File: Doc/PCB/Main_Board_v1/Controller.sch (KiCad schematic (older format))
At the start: 37 parts, among them J10 PTR1, J11 UART, J12 BUZZER, J7 Conn_01x02, J8 SP3, J9 SP2, Q2 IRLZ34N, Q3 IRLZ34N, U4 7805, U5 XPRESS-40, U6 LCD

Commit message: New Schemartics. Clean up monitor
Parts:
- removed C12: 4.7uF 50V, Capacitor_THT:C_Rect_L9.0mm_W3.3mm_P7.50mm_MKT, symbol Device:C
- removed C13: 100nF, Capacitor_THT:C_Rect_L9.0mm_W3.3mm_P7.50mm_MKT, symbol Device:C
- removed J7: Conn_01x02, Connector_PinHeader_2.54mm:PinHeader_1x02_P2.54mm_Horizontal, symbol Connector_Generic:Conn_01x02
- removed R14: 100, Resistor_THT:R_Axial_DIN0207_L6.3mm_D2.5mm_P10.16mm_Horizontal, symbol Device:R
- removed RV1: 5k, Resistor_THT:R_Axial_DIN0207_L6.3mm_D2.5mm_P10.16mm_Horizontal, symbol Device:R_POT
- removed U4: 7805, Package_TO_SOT_THT:TO-220-3_Vertical, symbol Power_Management:7805
- removed U5: XPRESS-40, symbol MCU_Microchip_PIC18:XPRESS-40
- removed U6: LCD, Connector_PinHeader_2.54mm:PinHeader_1x04_P2.54mm_Vertical, symbol LCD:LCD
- added C15: 4.7uF 50V, Capacitor_THT:CP_Radial_D5.0mm_P2.50mm, symbol Device:C
- added C16: 100nF, Capacitor_THT:C_Rect_L9.0mm_W3.3mm_P7.50mm_MKT, symbol Device:C
- added J12: I2C Interface LCD, Connector_PinHeader_2.54mm:PinHeader_1x04_P2.54mm_Vertical, symbol Connector:Conn_01x04_Male
- added J7: TE_3.5mm_Screwless_P2, Ventilator:PinHeader_1x02_Screwless_3.5mm, symbol Ventilator:TE_3.5mm_Screwless_P2
- added R15, R17: 470, Resistor_THT:R_Axial_DIN0207_L6.3mm_D2.5mm_P10.16mm_Horizontal, symbol Device:R
- added U4: LM7805_TO220, Package_TO_SOT_THT:TO-220-3_Vertical, symbol Regulator_Linear:LM7805_TO220
- added U5: XPRESS-40, Ventilator:EXPRESS-40_DIP_40, symbol Ventilator:XPRESS-40
- D2, D3: value 1N4001 -> 1N4007
- J10: footprint (none) -> Connector_PinHeader_2.54mm:PinHeader_1x03_P2.54mm_Vertical
- J11: footprint Connector_PinHeader_2.54mm:PinHeader_1x03_P2.54mm_Horizontal -> Connector_PinHeader_2.54mm:PinHeader_1x03_P2.54mm_Vertical
- J13: renamed from J12; value BUZZER -> BUZZER_C; footprint Connector_PinHeader_2.54mm:PinHeader_1x02_P2.54mm_Horizontal -> Connector_PinHeader_2.54mm:PinHeader_1x02_P2.54mm_Vertical
- J8, J9: footprint (none) -> Connector_PinHeader_2.54mm:PinHeader_1x02_P2.54mm_Vertical
- R13: renamed from R11; value R -> 50
- renumbered C15 to C17, C16 to C18, C17 to C19, R12 to R14, R13 to R16, R15 to R18, R16 to R19, R17 to R20, R18 to R21, R19 to R22, R20 to R23
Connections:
- net labels added: +12V_C, +5V_C, LCD_SCL, LCD_SDA
- net labels removed: +12V, +5V
- wire segments 176 -> 163
- no-connect marks 16 -> 19
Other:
- moved on the sheet: C19

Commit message: Update in the PCB design. New docs and images
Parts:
- removed J10: PTR1, Connector_PinHeader_2.54mm:PinHeader_1x03_P2.54mm_Vertical, symbol Connector:Conn_01x03_Male
- removed J8: SP3, Connector_PinHeader_2.54mm:PinHeader_1x02_P2.54mm_Vertical, symbol Connector:Screw_Terminal_01x02
- removed J9: SP2, Connector_PinHeader_2.54mm:PinHeader_1x02_P2.54mm_Vertical, symbol Connector:Screw_Terminal_01x02
- removed TP10: IP, Connector_PinHeader_2.54mm:PinHeader_1x02_P2.54mm_Vertical, symbol Connector:TestPoint_2Pole
- removed TP4: LED Breath, Connector_PinHeader_2.54mm:PinHeader_1x02_P2.54mm_Vertical, symbol Connector:TestPoint_2Pole
- removed TP5: Breath, Connector_PinHeader_2.54mm:PinHeader_1x02_P2.54mm_Vertical, symbol Connector:TestPoint_2Pole
- removed TP6: +, Connector_PinHeader_2.54mm:PinHeader_1x02_P2.54mm_Vertical, symbol Connector:TestPoint_2Pole
- removed TP7: -, Connector_PinHeader_2.54mm:PinHeader_1x02_P2.54mm_Vertical, symbol Connector:TestPoint_2Pole
- removed TP8: BPM, Connector_PinHeader_2.54mm:PinHeader_1x02_P2.54mm_Vertical, symbol Connector:TestPoint_2Pole
- removed TP9: EP, Connector_PinHeader_2.54mm:PinHeader_1x02_P2.54mm_Vertical, symbol Connector:TestPoint_2Pole
- added C22, C23, C24, C25, C26, C27: 1uF, Capacitor_THT:C_Rect_L7.0mm_W2.5mm_P5.00mm, symbol Device:C
- added C28, C29, C?: 100nF, Capacitor_THT:C_Rect_L9.0mm_W3.3mm_P7.50mm_MKT, symbol Device:C
- added J10: BPM, Ventilator:PushButton, symbol Ventilator:Button
- added J16: IP, Ventilator:PushButton, symbol Ventilator:Button
- added J17: -, Ventilator:PushButton, symbol Ventilator:Button
- added J18: BREATH, Ventilator:PushButton_LED, symbol Ventilator:Button_LED
- added J19: EP, Ventilator:PushButton, symbol Ventilator:Button
- added J20: +, Ventilator:PushButton, symbol Ventilator:Button
- added J8: SV2, Ventilator:PinHeader_1x02_Screwless_3.5mm, symbol Ventilator:TE_3.5mm_Screwless_P2
- added J9: SV3, Ventilator:PinHeader_1x02_Screwless_3.5mm, symbol Ventilator:TE_3.5mm_Screwless_P2
- added J?: VOL, Ventilator:PushButton, symbol Ventilator:Button
- added J?: VOL_MAX, Ventilator:PushButton, symbol Ventilator:Button
- added J?: VOL_MIN, Ventilator:PushButton, symbol Ventilator:Button
- added R26: 50, Resistor_THT:R_Axial_DIN0207_L6.3mm_D2.5mm_P10.16mm_Horizontal, symbol Device:R
- added R27, R28, R? (x3): 10k, Resistor_THT:R_Axial_DIN0207_L6.3mm_D2.5mm_P10.16mm_Horizontal, symbol Device:R
- added R29: 470, Resistor_THT:R_Axial_DIN0207_L6.3mm_D2.5mm_P10.16mm_Horizontal, symbol Device:R
- added S3, S4: MPXV5004DP, Ventilator:1351-01, symbol Ventilator:MPXV5004DP
- added TP5, TP6, TP7, TP8: TestPoint, Ventilator:LCD_DRILL, symbol Connector:TestPoint
- C17: value 1uF -> 100nF; footprint Capacitor_THT:C_Rect_L7.0mm_W2.5mm_P5.00mm -> Capacitor_THT:C_Rect_L9.0mm_W3.3mm_P7.50mm_MKT
- R13: value 50 -> 470
- R14: value R -> 50
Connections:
- net labels added: PR2, PR3, SV2, SV3
- wire segments 163 -> 248
- no-connect marks 19 -> 14
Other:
- moved on the sheet: J13, R16

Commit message: First placement of board
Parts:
- added J24: Conn_01x08, Connector_PinHeader_2.54mm:PinHeader_1x08_P2.54mm_Horizontal, symbol Connector_Generic:Conn_01x08
- added R36: 10k, Resistor_THT:R_Axial_DIN0207_L6.3mm_D2.5mm_P10.16mm_Horizontal, symbol Device:R
- C14, C16, C17, C19, C28, C29: value 100nF -> 100nF - 100V; footprint Capacitor_THT:C_Rect_L9.0mm_W3.3mm_P7.50mm_MKT -> Capacitor_THT:C_Rect_L7.2mm_W2.5mm_P5.00mm_FKS2_FKP2_MKS2_MKP2
- C15: footprint Capacitor_THT:CP_Radial_D5.0mm_P2.50mm -> Capacitor_THT:CP_Radial_D5.0mm_P2.00mm
- C18, C22, C23, C24, C25, C26, C27: footprint Capacitor_THT:C_Rect_L7.0mm_W2.5mm_P5.00mm -> Capacitor_THT:C_Rect_L13.0mm_W4.0mm_P10.00mm_FKS3_FKP3_MKS4
- C30: renamed from C?; value 100nF -> 100nF - 100V; footprint Capacitor_THT:C_Rect_L9.0mm_W3.3mm_P7.50mm_MKT -> Capacitor_THT:C_Rect_L7.2mm_W2.5mm_P5.00mm_FKS2_FKP2_MKS2_MKP2
- J12: value I2C Interface LCD -> I2C Interface LCD_C; footprint Connector_PinHeader_2.54mm:PinHeader_1x04_P2.54mm_Vertical -> Ventilator:PH_4_pol
- gave numbers to parts that had none: 6
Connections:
- net +5V_C: now also J24.2 (Pin_2), R36.1
- net GND: now also J24.3 (Pin_3)
- net nMCLR_C: now reaches U5.1 (RE3)
- net nMCLR_C: now also J24.1 (Pin_1), R36.2
- net ICSPCLK_C: now reaches U5.39 (TGCLK)
- net ICSPCLK_C: now also J24.5 (Pin_5)
- net ICSPDAT_C: now reaches U5.40 (TGDAT)
- net ICSPDAT_C: now also J24.4 (Pin_4)
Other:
- moved on the sheet: C29, J12, R15, R17

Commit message: Update in PCB: Schematic and Layout
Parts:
- added TP10, TP11, TP12, TP13: TestPoint, Ventilator:LCD_DRILL, symbol Connector:TestPoint
- Q2, Q3: value IRLZ34N -> STP24NF10
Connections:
- net GND: now also TP10.1, TP11.1, TP12.1, TP13.1
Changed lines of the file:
@@
 AR Path="/5E9339D0/5EC06140" Ref="Q2"  Part="1"
 F 0 "Q2" H 2954 5096 50  0000 L CNN
-F 1 "IRLZ34N" H 2954 5005 50  0000 L CNN
+F 1 "STP24NF10 " H 2954 5005 50  0000 L CNN
 F 2 "Package_TO_SOT_THT:TO-220-3_Vertical" H 3000 4975 50  0001 L CIN
-F 3 "http://www.infineon.com/dgdl/irlz34npbf.pdf?fileId=5546d462533600a40153567206892720" H 2750 5050 50  0001 L CNN
+F 3 "https://es.rs-online.com/web/p/mosfet/6875377/" H 2750 5050 50  0001 L CNN
 	1    2750 5050
 	-1   0    0    -1
@@
 F 1 "SV2" V 1974 4267 50  0000 C CNN
 F 2 "Ventilator:PinHeader_1x02_Screwless_3.5mm" H 1650 4650 50  0001 C CNN
-F 3 "" H 1650 4650 50  0001 C CNN
+F 3 "https://es.rs-online.com/web/p/bloques-terminales-para-pcb/1232052/" H 1650 4650 50  0001 C CNN
 	1    1650 4300
 	0    -1   1    0
@@
 AR Path="/5E9339D0/5ECD870B" Ref="Q3"  Part="1"
 F 0 "Q3" H 2954 7046 50  0000 L CNN
-F 1 "IRLZ34N" H 2954 6955 50  0000 L CNN
+F 1 "STP24NF10 " H 2954 6955 50  0000 L CNN
 F 2 "Package_TO_SOT_THT:TO-220-3_Vertical" H 3000 6925 50  0001 L CIN
-F 3 "http://www.infineon.com/dgdl/irlz34npbf.pdf?fileId=5546d462533600a40153567206892720" H 2750 7000 50  0001 L CNN
+F 3 "https://es.rs-online.com/web/p/mosfet/6875377/" H 2750 7000 50  0001 L CNN
 	1    2750 7000
 	-1   0    0    -1
@@
 F 1 "SV3" V 1974 6217 50  0000 C CNN
 F 2 "Ventilator:PinHeader_1x02_Screwless_3.5mm" H 1650 6600 50  0001 C CNN
-F 3 "" H 1650 6600 50  0001 C CNN
+F 3 "https://es.rs-online.com/web/p/bloques-terminales-para-pcb/1232052/" H 1650 6600 50  0001 C CNN
 	1    1650 6250
 	0    -1   1    0
@@
 F 1 "-" H 10628 4455 50  0000 L CNN
 F 2 "Ventilator:PushButton" H 10300 4500 50  0001 C CNN
-F 3 "" H 10300 4500 50  0001 C CNN
+F 3 "https://es.rs-online.com/web/p/botones-pulsadores/7346827/" H 10300 4500 50  0001 C CNN
 	1    10300 4500
 	1    0    0    -1
@@
 F 1 "+" H 11028 4155 50  0000 L CNN
 F 2 "Ventilator:PushButton" H 10700 4200 50  0001 C CNN
-F 3 "" H 10700 4200 50  0001 C CNN
+F 3 "https://es.rs-online.com/web/p/botones-pulsadores/7346827/" H 10700 4200 50  0001 C CNN
 	1    10700 4200
 	1    0    0    -1
@@
 F 1 "IP" H 10628 3855 50  0000 L CNN
 F 2 "Ventilator:PushButton" H 10300 3900 50  0001 C CNN
-F 3 "" H 10300 3900 50  0001 C CNN
+F 3 "https://es.rs-online.com/web/p/botones-pulsadores/7346827/" H 10300 3900 50  0001 C CNN
 	1    10300 3900
 	1    0    0    -1
@@
 F 1 "EP" H 11028 3555 50  0000 L CNN
 F 2 "Ventilator:PushButton" H 10700 3600 50  0001 C CNN
-F 3 "" H 10700 3600 50  0001 C CNN
+F 3 "https://es.rs-online.com/web/p/botones-pulsadores/7346827/" H 10700 3600 50  0001 C CNN
 	1    10700 3600
 	1    0    0    -1
@@
 F 1 "BPM" H 10628 3255 50  0000 L CNN
 F 2 "Ventilator:PushButton" H 10300 3300 50  0001 C CNN
-F 3 "" H 10300 3300 50  0001 C CNN
+F 3 "https://es.rs-online.com/web/p/botones-pulsadores/7346827/" H 10300 3300 50  0001 C CNN
 	1    10300 3300
 	1    0    0    -1
@@
 F 1 "VOL" H 10428 5905 50  0000 L CNN
 F 2 "Ventilator:PushButton" H 10100 5950 50  0001 C CNN
-F 3 "" H 10100 5950 50  0001 C CNN
+F 3 "https://es.rs-online.com/web/p/botones-pulsadores/7346827/" H 10100 5950 50  0001 C CNN
 	1    10100 5950
 	1    0    0    -1
@@
 F 1 "VOL_MAX" H 10828 5605 50  0000 L CNN
 F 2 "Ventilator:PushButton" H 10500 5650 50  0001 C CNN
-F 3 "" H 10500 5650 50  0001 C CNN
+F 3 "https://es.rs-online.com/web/p/botones-pulsadores/7346827/" H 10500 5650 50  0001 C CNN
 	1    10500 5650
 	1    0    0    -1
@@
 F 1 "VOL_MIN" H 10428 5305 50  0000 L CNN
 F 2 "Ventilator:PushButton" H 10100 5350 50  0001 C CNN
-F 3 "" H 10100 5350 50  0001 C CNN
+F 3 "https://es.rs-online.com/web/p/botones-pulsadores/7346827/" H 10100 5350 50  0001 C CNN
 	1    10100 5350
 	1    0    0    -1
@@
 Wire Wire Line
 	4900 1850 5500 1850
+$Comp
+L Connector:TestPoint TP?
+U 1 1 5F66F306
+P 5400 6200
+AR Path="/5E9337AC/5F66F306" Ref="TP?"  Part="1"
+AR Path="/5E9339D0/5F66F306" Ref="TP12"  Part="1"
+F 0 "TP12" H 5458 6318 50  0000 L CNN
+F 1 "TestPoint" H 5458 6227 50  0000 L CNN
+F 2 "Ventilator:LCD_DRILL" H 5600 6200 50  0001 C CNN
+F 3 "~" H 5600 6200 50  0001 C CNN
+	1    5400 6200
+	1    0    0    -1
+$EndComp
+$Comp
+L Connector:TestPoint TP?
+U 1 1 5F66F30C
+P 4950 6200
+AR Path="/5E9337AC/5F66F30C" Ref="TP?"  Part="1"
+AR Path="/5E9339D0/5F66F30C" Ref="TP11"  Part="1"
+F 0 "TP11" H 5008 6318 50  0000 L CNN
+F 1 "TestPoint" H 5008 6227 50  0000 L CNN
+F 2 "Ventilator:LCD_DRILL" H 5150 6200 50  0001 C CNN
+F 3 "~" H 5150 6200 50  0001 C CNN
+	1    4950 6200
+	1    0    0    -1
+$EndComp
+$Comp
+L Connector:TestPoint TP?
+U 1 1 5F66F312
+P 4500 6200
+AR Path="/5E9337AC/5F66F312" Ref="TP?"  Part="1"
+AR Path="/5E9339D0/5F66F312" Ref="TP10"  Part="1"
+F 0 "TP10" H 4558 6318 50  0000 L CNN
+F 1 "TestPoint" H 4558 6227 50  0000 L CNN
+F 2 "Ventilator:LCD_DRILL" H 4700 6200 50  0001 C CNN
+F 3 "~" H 4700 6200 50  0001 C CNN
+	1    4500 6200
+	1    0    0    -1
+$EndComp
+$Comp
+L Connector:TestPoint TP?
+U 1 1 5F66F318
+P 5850 6200
+AR Path="/5E9337AC/5F66F318" Ref="TP?"  Part="1"
+AR Path="/5E9339D0/5F66F318" Ref="TP13"  Part="1"
+F 0 "TP13" H 5908 6318 50  0000 L CNN
+F 1 "TestPoint" H 5908 6227 50  0000 L CNN
+F 2 "Ventilator:LCD_DRILL" H 6050 6200 50  0001 C CNN
+F 3 "~" H 6050 6200 50  0001 C CNN
+	1    5850 6200
+	1    0    0    -1
+$EndComp
+$Comp
+L power:GND #PWR?
+U 1 1 5F66F31E
+P 5250 6600
+AR Path="/5F66F31E" Ref="#PWR?"  Part="1"
+AR Path="/5EA602EB/5F66F31E" Ref="#PWR?"  Part="1"
+AR Path="/5E9337AC/5F66F31E" Ref="#PWR?"  Part="1"
+AR Path="/5E9339D0/5F66F31E" Ref="#PWR0127"  Part="1"
+F 0 "#PWR0127" H 5250 6350 50  0001 C CNN
+F 1 "GND" H 5255 6427 50  0000 C CNN
+F 2 "" H 5250 6600 50  0001 C CNN
+F 3 "" H 5250 6600 50  0001 C CNN
+	1    5250 6600
+	1    0    0    -1
+$EndComp
+Wire Wire Line
+	4500 6200 4500 6450
+Wire Wire Line
+	4500 6450 4950 6450
+Wire Wire Line
+	5250 6450 5250 6600
+Wire Wire Line
+	5850 6450 5400 6450
+Wire Wire Line
+	5850 6200 5850 6450
+Connection ~ 5250 6450
+Wire Wire Line
+	5400 6200 5400 6450
+Connection ~ 5400 6450
+Wire Wire Line
+	5400 6450 5250 6450
+Wire Wire Line
+	4950 6200 4950 6450
+Connection ~ 4950 6450
+Wire Wire Line
+	4950 6450 5250 6450
 $EndSCHEMATC

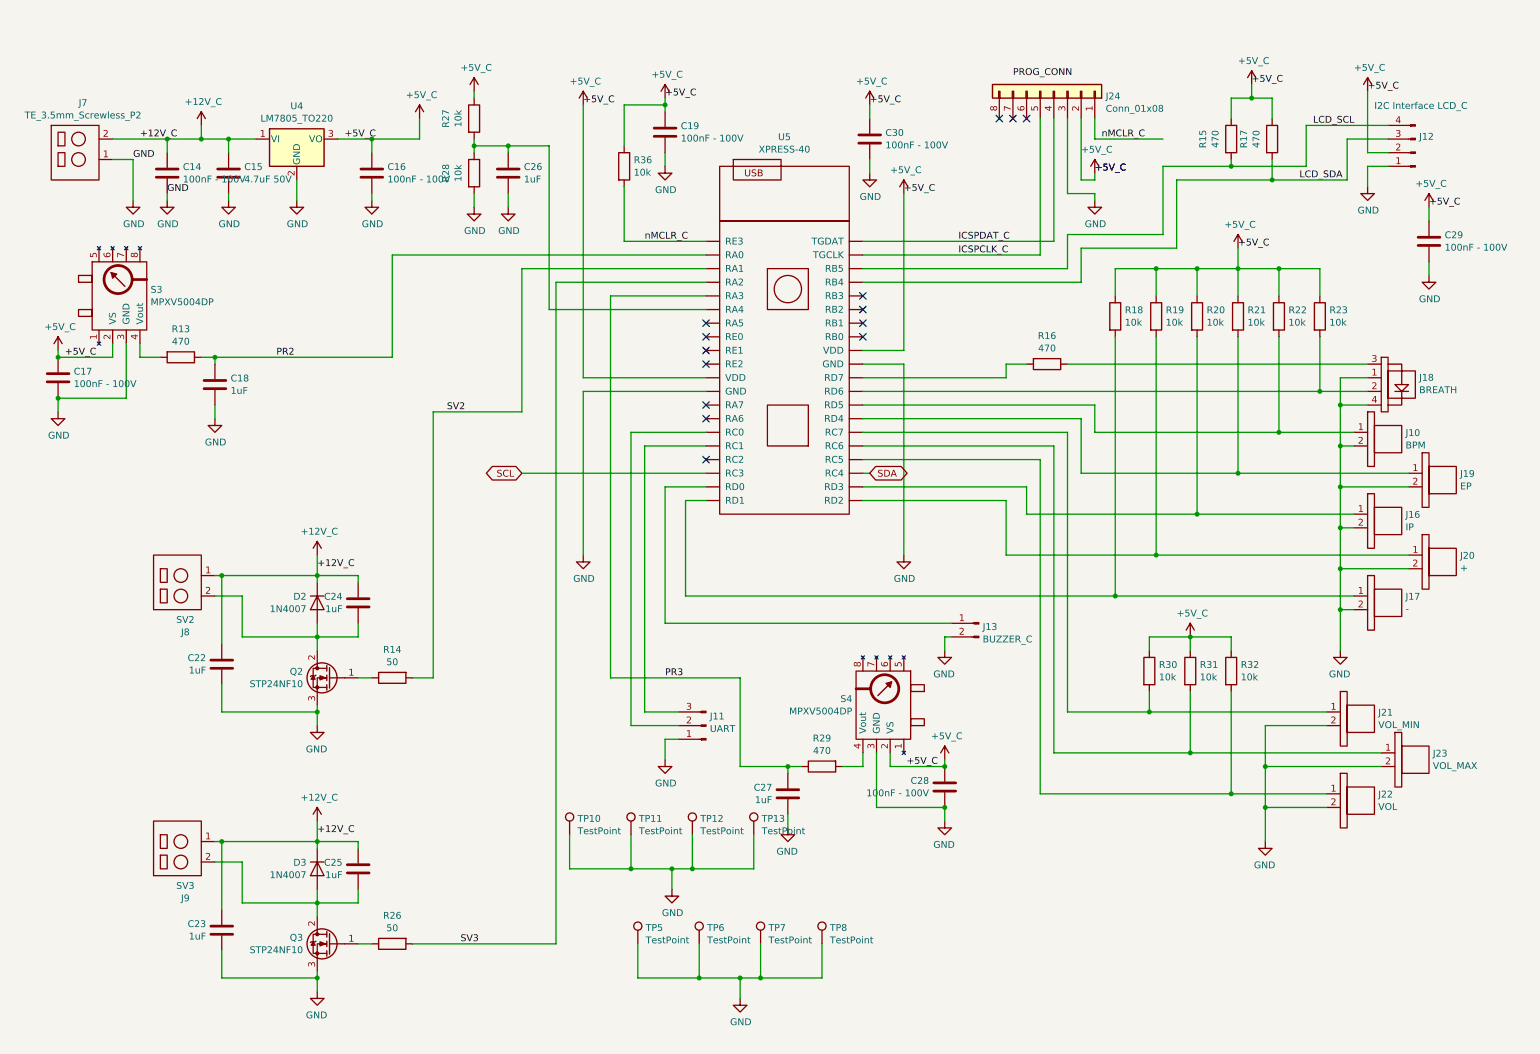
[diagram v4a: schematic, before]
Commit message: New PCB version; I2C Slave works
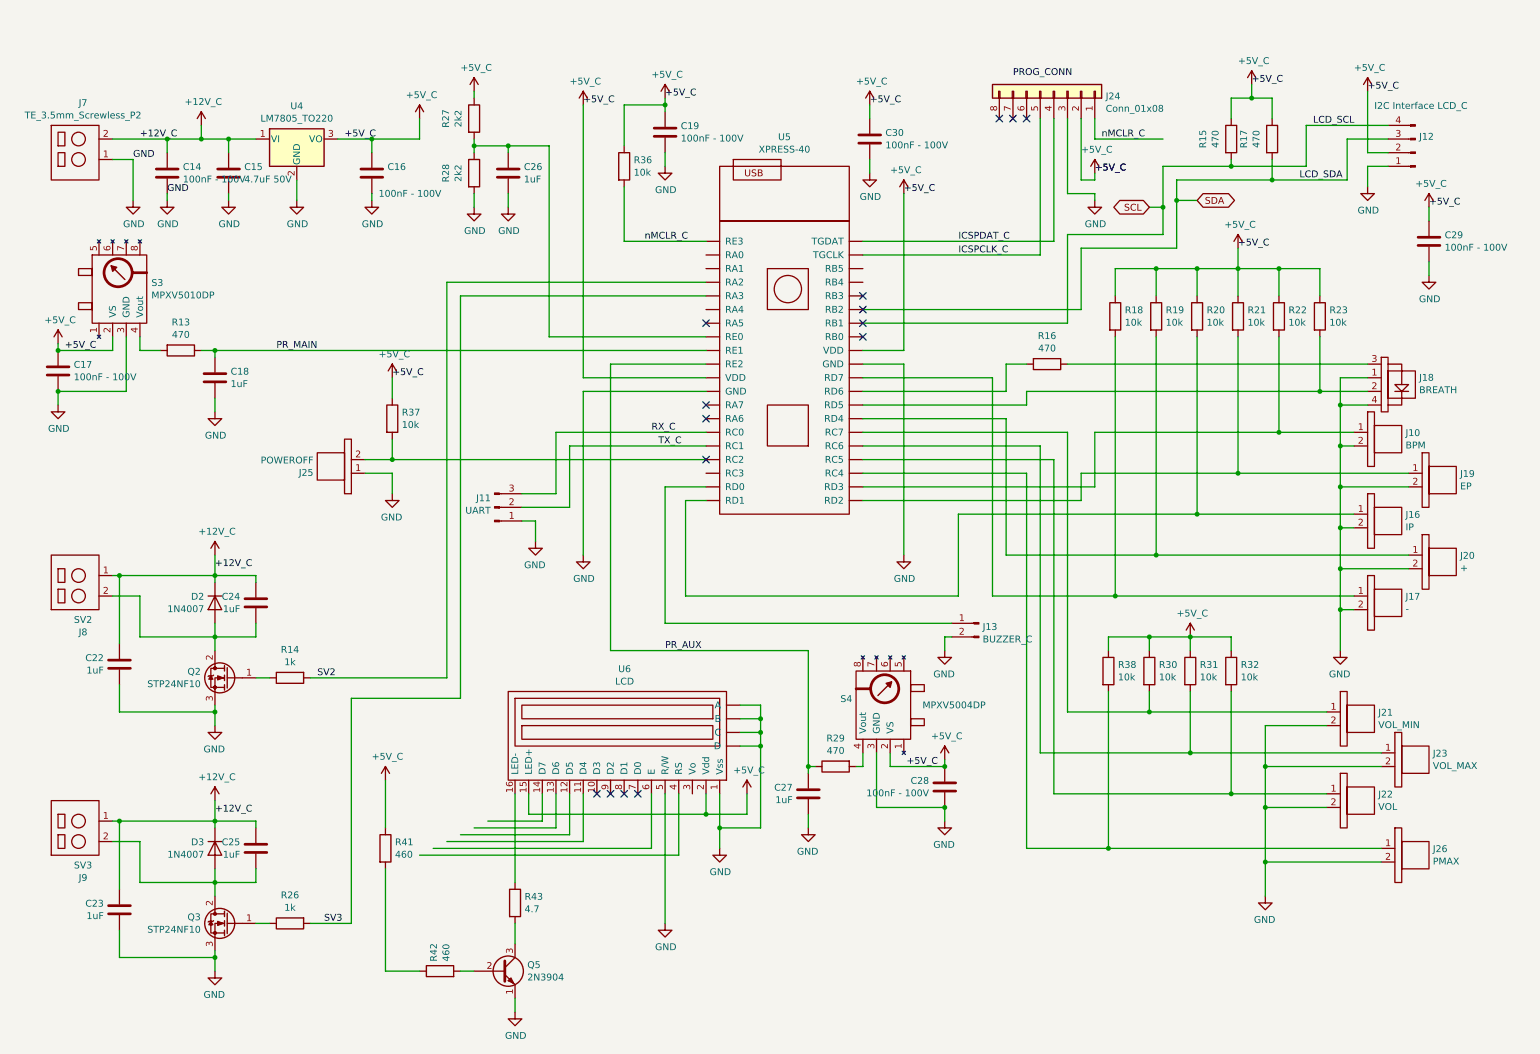
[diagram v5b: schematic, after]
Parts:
- removed S3: MPXV5004DP, Ventilator:1351-01, symbol Ventilator:MPXV5004DP
- removed TP10, TP11, TP12, TP13, TP5, TP6, TP7, TP8: TestPoint, Ventilator:LCD_DRILL, symbol Connector:TestPoint
- added J25: POWEROFF, Ventilator:PushButton, symbol Ventilator:Button
- added J26: PMAX, Ventilator:PushButton, symbol Ventilator:Button
- added Q5: 2N3904, Package_TO_SOT_THT:TO-92_Inline, symbol Transistor_BJT:2N3904
- added R37, R38: 10k, Resistor_THT:R_Axial_DIN0207_L6.3mm_D2.5mm_P10.16mm_Horizontal, symbol Device:R
- added R41, R42: 460, Resistor_THT:R_Axial_DIN0207_L6.3mm_D2.5mm_P10.16mm_Horizontal, symbol Device:R
- added R43: 4.7, Resistor_THT:R_Axial_DIN0207_L6.3mm_D2.5mm_P10.16mm_Horizontal, symbol Device:R
- added S3: MPXV5010DP, Ventilator:1351-01, symbol Ventilator:MPXV5010DP
- added U6: LCD, Ventilator:LCD_2x16, symbol Ventilator:LCD
- R14, R26: value 50 -> 1k
- R27, R28: value 10k -> 2k2
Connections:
- net +5V_C: now also R37.1, R38.1, R41.1, S3.2 (VS), U6.15 (LED+), U6.2 (Vdd)
- net GND: now also J25.1, J26.2, Q5.1 (E), S3.3 (GND), U6.1 (Vss), U6.5 (R/W), U6.~ (D)
- net SCL: now also J12.4 (Pin_4), R15.2, U5.34 (RB1); no longer U5.18 (RC3)
- net SDA: now also J12.3 (Pin_3), R17.2, U5.35 (RB2); no longer U5.23 (RC4)
- net SV2: now also U5.4 (RA2); no longer U5.3 (RA1)
- net SV3: now also U5.5 (RA3); no longer U5.4 (RA2)
- net at R13.2: now also S3.4 (Vout)
- net at J18.2, R23.2: now also U5.28 (RD5); no longer U5.29 (RD6)
- net at J17.1, R18.2: now also U5.30 (RD7); no longer U5.20 (RD1)
- net at R16.2: now also U5.29 (RD6); no longer U5.30 (RD7)
- net at J20.1, R19.2: now also U5.27 (RD4); no longer U5.21 (RD2)
- net at J16.1, R20.2: now also U5.20 (RD1); no longer U5.22 (RD3)
- net at J19.1, R21.2: now also U5.21 (RD2); no longer U5.27 (RD4)
- net at J10.1, R22.2: now also U5.22 (RD3); no longer U5.28 (RD5)
- net at C26.1, R27.2, R28.1: now also U5.8 (RE0); no longer U5.6 (RA4)
- net PR_AUX: now reaches U5.10 (RE2)
- net PR_AUX: now also C27.1, R29.1
- net RX_C: now reaches U5.15 (RC0)
- net RX_C: now also J11.3 (Pin_3); no longer J11.2 (Pin_2)
- net TX_C: now reaches U5.16 (RC1)
- net TX_C: now also J11.2 (Pin_2); no longer J11.3 (Pin_3)
- net at U5.17 (RC2): now also J25.2, R37.2
- net PR_MAIN: now reaches U5.9 (RE1)
- net PR_MAIN: now also C18.1, R13.1
- removed net LCD_SCL: J12.4 (Pin_4), R15.2, U5.38 (RB5)
- removed net LCD_SDA: J12.3 (Pin_3), R17.2, U5.37 (RB4)
- removed net PR2: C18.1, R13.1, U5.2 (RA0)
- removed net PR3: C27.1, R29.1, U5.5 (RA3)
- new net: J26.1, R38.2, U5.23 (RC4)
- new net: R43.1, U6.16 (LED-)
- new net: Q5.2 (B), R42.2
- new net: Q5.3 (C), R43.2
- new net: R41.2, R42.1
- no-connect marks 14 -> 15
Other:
- moved on the sheet: C17, C18, C22, C23, C24, C25, C27, D2, D3, J11, J8, J9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
